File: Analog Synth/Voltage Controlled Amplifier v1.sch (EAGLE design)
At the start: 45 parts, among them IC1 TL084P, IC2 TL084P, IC3 TL084P, IC4 CA3046, IC5 78L05Z, IC6 79L05

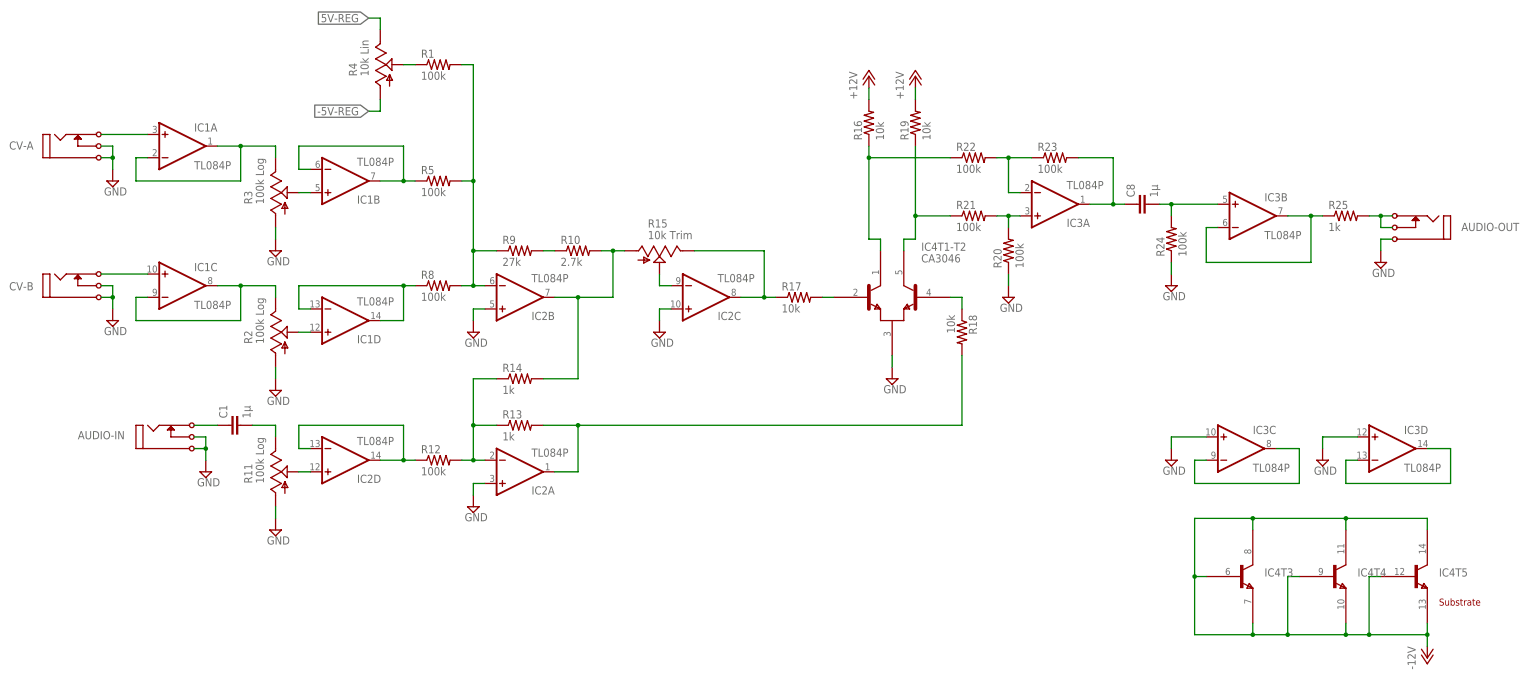
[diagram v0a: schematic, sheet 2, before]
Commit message: working on VCA-v1
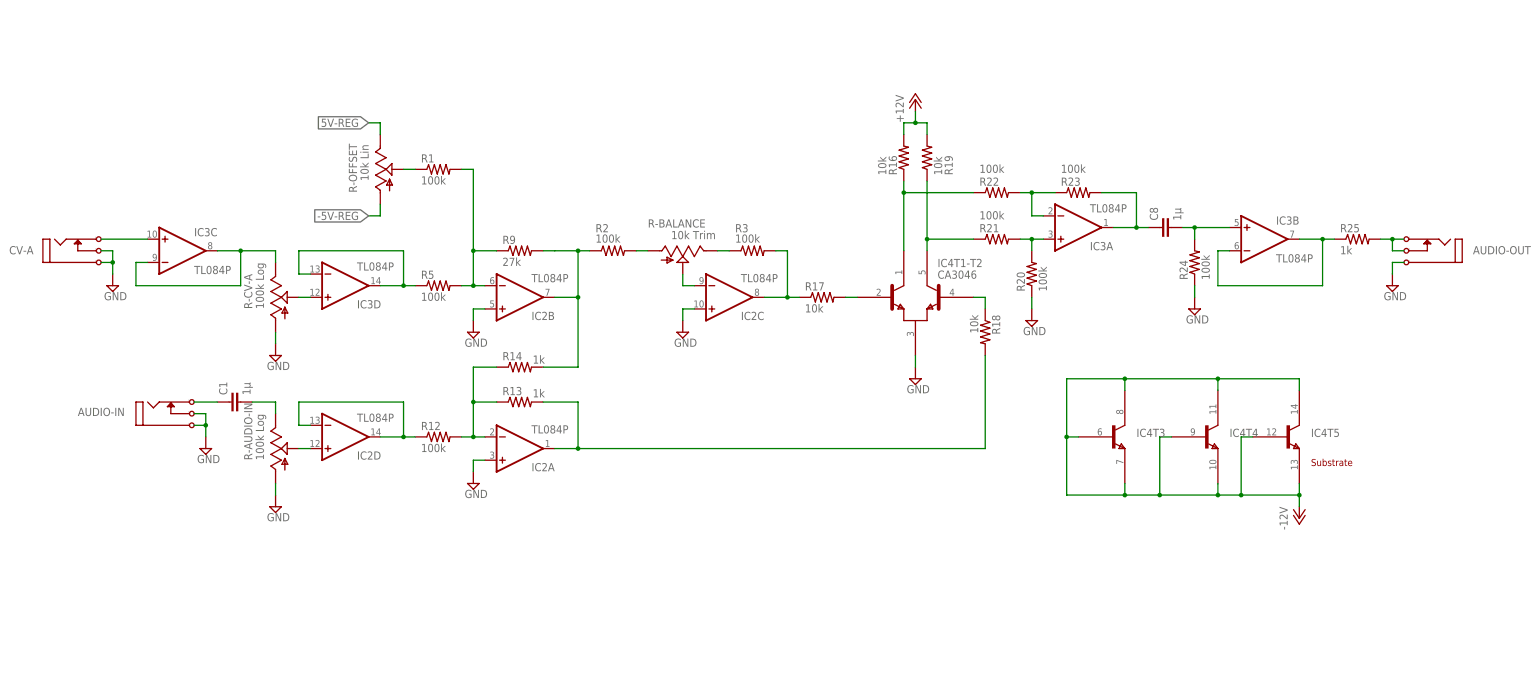
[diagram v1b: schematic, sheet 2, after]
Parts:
- removed CV-B: I/O, !synth_sch:MONO_JACK
- removed IC1: TL084P, linear:TL084P
- removed R10: 2.7k, resistor:R-US_0204/7
- removed R11: 100k Log, pot:TRIM_US-B64Y
- removed R15: 10k Trim, pot:TRIM_US-B64Y
- removed R4: 10k Lin, pot:TRIM_US-B64Y
- removed R8: 100k, resistor:R-US_0204/7
- added R-AUDIO-IN, R-CV-A: 100k Log, pot:TRIM_US-B64Y
- added R-BALANCE: 10k Trim, pot:TRIM_US-B64Y
- added R-OFFSET: 10k Lin, pot:TRIM_US-B64Y
- R2, R3: value 100k Log -> 100k; device pot:TRIM_US-B64Y -> resistor:R-US_0204/7
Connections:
- removed net N$35: IC3C.-IN, IC3C.OUT
- removed net N$36: IC3D.-IN, IC3D.OUT
- removed net N$8: IC1D.+IN, R2.S
- removed net N$9: IC1D.-IN, IC1D.OUT, R8.1
- net -5V-REG: now also R-OFFSET.A; no longer R4.A
- net 5V-REG: now also R-OFFSET.E; no longer R4.E
- net GND: now also R-AUDIO-IN.A, R-CV-A.A; no longer CV-B.P$1, CV-B.P3, IC3C.+IN, IC3D.+IN, R11.A, R2.A, R3.A
- net N$1: now also IC3D.-IN, IC3D.OUT; no longer IC1B.-IN, IC1B.OUT
- net N$13: now also R-OFFSET.S
- net N$14: now also IC3D.+IN, R-CV-A.S; no longer IC1B.+IN, R3.S
- net N$15: now also R2.1; no longer R10.2, R15.A
- net N$16: no longer R10.1
- net N$19: now also R-AUDIO-IN.S; no longer R11.S
- net N$20: now also R-AUDIO-IN.E; no longer R11.E
- net N$23: now also R3.2; no longer R15.E
- net N$25: now also R-BALANCE.S; no longer R15.S
- net N$3: now also IC3C.+IN; no longer IC1A.+IN
- net N$4: now also IC3C.-IN, IC3C.OUT, R-CV-A.E; no longer IC1A.-IN, IC1A.OUT, R3.E
- net N$5: now also R-BALANCE.E, R3.1; no longer CV-B.P2, IC1C.+IN
- net N$6: no longer R8.2
- net N$7: now also R-BALANCE.A, R2.2; no longer IC1C.-IN, IC1C.OUT, R2.E
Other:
- moved on the sheet: AUDIO-IN, AUDIO-OUT, C1, C8, CV-A, IC2A, IC2C, IC2D, IC3A, IC3B, IC3C, IC3D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

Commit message: working on Power Distribution and VCA.
When playing with my VCA on my bench, I discovered it can be used as an AM radio to pick up a local station on 1420 kHz (KTOE in Mankato)
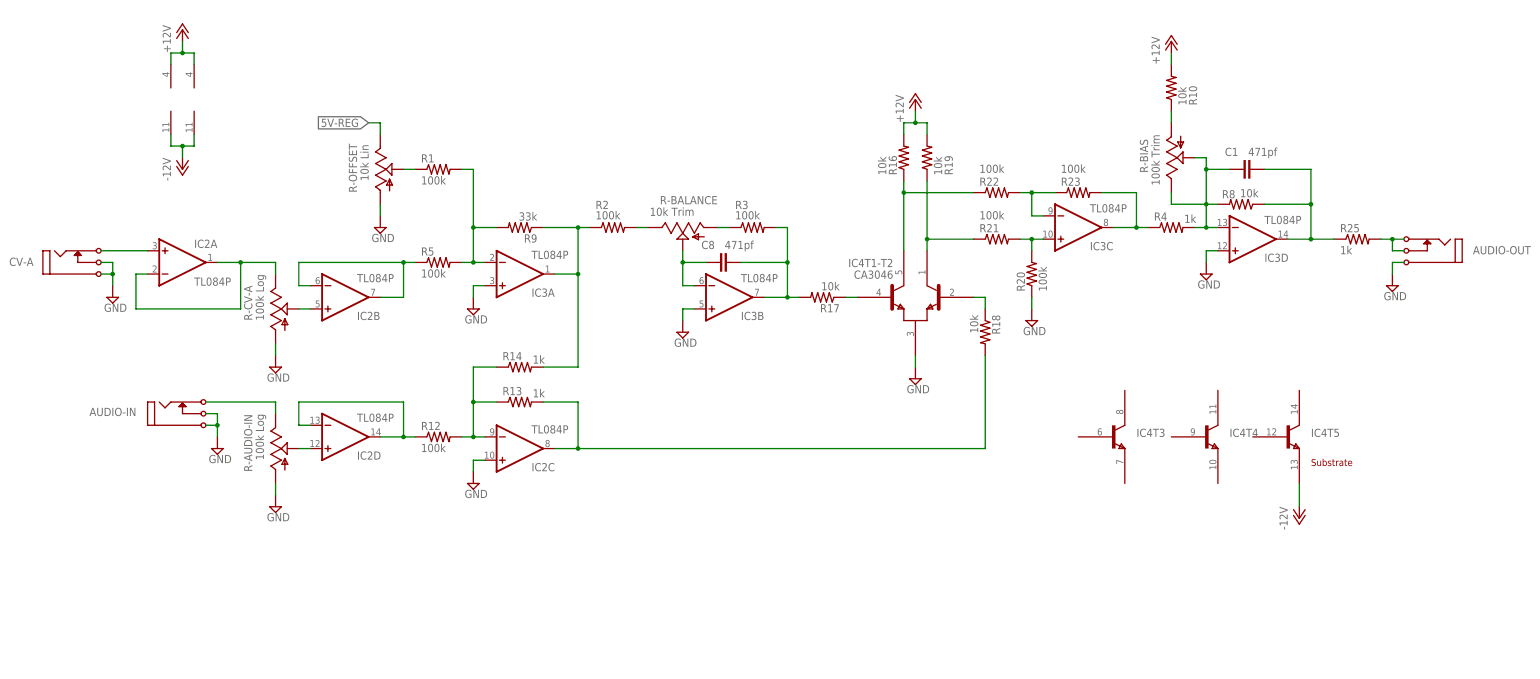
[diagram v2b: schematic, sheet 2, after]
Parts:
- removed C4, C5: 10µ, rcl:C-US025-050X050
- removed IC5: 78L05Z, linear:78L05Z
- removed IC6: 79L05, linear:79L05Z
- removed R24: 100k, resistor:R-US_0204/7
- removed U$3, U$7: POWER_CONNECTOR_4_RGBB, !synth_sch:POWER_CONNECTOR_4_RGBB
- added R-BIAS: 100k Trim, pot:TRIM_US-B64Y
- added R10, R8: 10k, resistor:R-US_0204/2V
- added R4: 1k, resistor:R-US_0204/2V
- added U$1: EURORACK-POWER, !synth_sch:EURORACK-POWER
- C1, C8: value 1µ -> 471pf
- R1, R12, R13, R14, R16, R17, R19, R2, R20, R21, R22, R23, R3, R5: device resistor:R-US_0204/7 -> resistor:R-US_0204/2V
- R9: value 27k -> 33k; device resistor:R-US_0204/7 -> resistor:R-US_0204/2V
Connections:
- removed net -5V-REG: C5.2, C7.2, IC6.VO, R-OFFSET.A
- removed net N$11: U$3.+5, U$7.+5
- removed net N$12: R6.2, U$3.-12, U$7.-12
- removed net N$17: AUDIO-IN.P2, C1.1
- removed net N$29: C8.2, IC3B.+IN, R24.2
- new net N$8: R6.2, U$1.P$10, U$1.P$9
- new net N$9: AUDIO-IN.P2, R-AUDIO-IN.E
- net +12V: now also C6.1, IC2P.V+, IC3P.V+, R10.2; no longer IC5.VI
- net -12V: now also C7.2, IC2P.V-, IC3P.V-; no longer IC4T3.B, IC4T3.C, IC4T3.E, IC4T4.B, IC4T4.C, IC4T4.E, IC4T5.B, IC4T5.C, IC6.VI
- net 5V-REG: no longer C4.1, C6.1, IC5.VO
- net GND: now also IC3A.+IN, IC3B.+IN, IC3D.+IN, R-OFFSET.A, U$1.P$3, U$1.P$4, U$1.P$5, U$1.P$6, U$1.P$7, U$1.P$8; no longer C4.2, C5.1, IC2A.+IN, IC2B.+IN, IC5.GND, IC6.GND, R24.1, U$3.GND, U$7.GND
- net N$1: now also IC2B.-IN, IC2B.OUT; no longer IC3D.-IN, IC3D.OUT
- net N$10: now also U$1.P$1, U$1.P$2; no longer U$3.+12, U$7.+12
- net N$14: now also IC2B.+IN; no longer IC3D.+IN
- net N$15: now also IC3A.OUT, R9.1; no longer IC2B.OUT
- net N$16: now also R-BIAS.A, R10.1; no longer R9.2
- net N$2: now also IC4T1-T2.B2, R17.1; no longer IC4T1-T2.B1, R17.2
- net N$20: now also C1.1, IC3D.-IN, R-BIAS.E, R-BIAS.S, R4.2, R8.2; no longer C1.2, R-AUDIO-IN.E
- net N$21: now also IC4T1-T2.B1; no longer IC4T1-T2.B2
- net N$22: now also IC2C.-IN; no longer IC2A.-IN
- net N$23: now also C8.2, IC3B.OUT, R17.2; no longer IC2C.OUT, R17.1
- net N$24: now also IC4T1-T2.C2; no longer IC4T1-T2.C1
- net N$25: now also C8.1, IC3B.-IN; no longer IC2C.-IN
- net N$26: now also IC4T1-T2.C1; no longer IC4T1-T2.C2
- net N$27: now also IC2C.OUT; no longer IC2A.OUT
- net N$28: now also IC3C.+IN; no longer IC3A.+IN
- net N$3: now also IC2A.+IN; no longer IC3C.+IN
- net N$30: now also IC3C.-IN; no longer IC3A.-IN
- net N$31: now also IC3C.OUT, R4.1; no longer C8.1, IC3A.OUT
- net N$34: now also C1.2, IC3D.OUT, R8.1; no longer IC3B.-IN, IC3B.OUT
- net N$4: now also IC2A.-IN, IC2A.OUT; no longer IC3C.-IN, IC3C.OUT
- net N$5: now also R2.2; no longer R3.1
- net N$6: now also IC3A.-IN, R9.2; no longer IC2B.-IN, R9.1
- net N$7: now also R3.1; no longer R2.2
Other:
- moved on the sheet: AUDIO-IN, C1, C6, C7, C8, CV-A, IC2A, IC2B, IC2C, IC3A, IC3B, IC3C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
